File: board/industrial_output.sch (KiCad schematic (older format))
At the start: 3 parts, among them Q1501 NJT4031NT1G

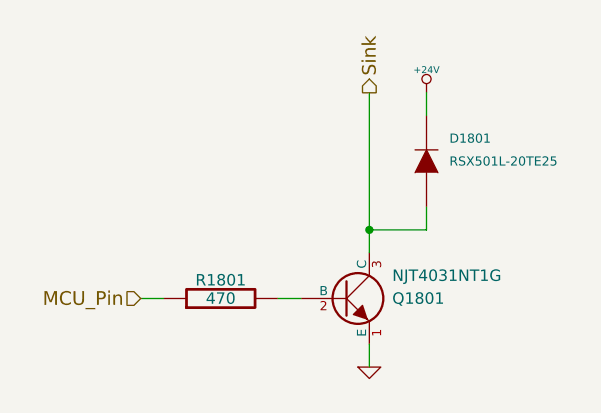
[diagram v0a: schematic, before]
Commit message: Selected Part Numbers for all Components
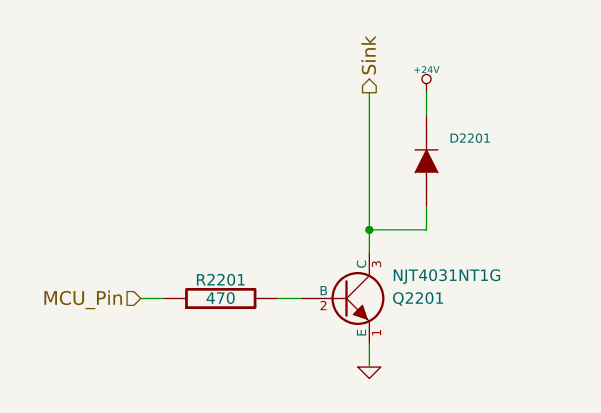
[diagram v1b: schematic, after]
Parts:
- D1501: Part Number (none) -> RSX501L-20TE25
- Q1501: Part Number (none) -> NJT4031NT1G
- R1501: Part Number (none) -> RC1608J471CS
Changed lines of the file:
@@
 $Descr A 11000 8500
 encoding utf-8
-Sheet 18 26
+Sheet 15 26
 Title "Industrial Digital Output"
 Date ""
@@
 AR Path="/52FAF275/52E6FDE0" Ref="Q2101"  Part="1"
 AR Path="/52FAF279/52E6FDE0" Ref="Q2201"  Part="1"
-F 0 "Q1801" H 5650 4500 50  0000 L CNN
+F 0 "Q2201" H 5650 4500 50  0000 L CNN
 F 1 "NJT4031NT1G" H 5650 4600 50  0000 L CNN
 F 2 "" H 5450 4500 60  0000 C CNN
 F 3 "" H 5450 4500 60  0000 C CNN
+F 4 "NJT4031NT1G" H 5450 4500 60  0001 C CNN "Part Number"
 	1    5450 4500
 	1    0    0    -1
@@
 AR Path="/52FAF275/52E6FDF4" Ref="R2101"  Part="1"
 AR Path="/52FAF279/52E6FDF4" Ref="R2201"  Part="1"
-F 0 "R1801" V 4980 4500 50  0000 C CNN
+F 0 "R2201" V 4980 4500 50  0000 C CNN
 F 1 "470" V 4900 4500 50  0000 C CNN
 F 2 "" H 4900 4500 60  0000 C CNN
 F 3 "" H 4900 4500 60  0000 C CNN
+F 4 "RC1608J471CS" V 4900 4500 60  0001 C CNN "Part Number"
 	1    4900 4500
 	0    -1   -1   0
@@
 	5150 4500 5250 4500
 $Comp
-L GND #PWR0160
+L GND #PWR0165
 U 1 1 52E6FE0A
 P 5550 4800
-AR Path="/52FAAFCB/52E6FE0A" Ref="#PWR0160"  Part="1"
-AR Path="/52FAC46B/52E6FE0A" Ref="#PWR0162"  Part="1"
-AR Path="/52FAD3BD/52E6FE0A" Ref="#PWR0164"  Part="1"
-AR Path="/52FAD3C1/52E6FE0A" Ref="#PWR0166"  Part="1"
-AR Path="/52FAF26D/52E6FE0A" Ref="#PWR0168"  Part="1"
-AR Path="/52FAF271/52E6FE0A" Ref="#PWR0170"  Part="1"
-AR Path="/52FAF275/52E6FE0A" Ref="#PWR0172"  Part="1"
-AR Path="/52FAF279/52E6FE0A" Ref="#PWR0174"  Part="1"
-F 0 "#PWR0166" H 5550 4800 30  0001 C CNN
+AR Path="/52FAAFCB/52E6FE0A" Ref="#PWR0165"  Part="1"
+AR Path="/52FAC46B/52E6FE0A" Ref="#PWR0167"  Part="1"
+AR Path="/52FAD3BD/52E6FE0A" Ref="#PWR0169"  Part="1"
+AR Path="/52FAD3C1/52E6FE0A" Ref="#PWR0171"  Part="1"
+AR Path="/52FAF26D/52E6FE0A" Ref="#PWR0173"  Part="1"
+AR Path="/52FAF271/52E6FE0A" Ref="#PWR0175"  Part="1"
+AR Path="/52FAF275/52E6FE0A" Ref="#PWR0177"  Part="1"
+AR Path="/52FAF279/52E6FE0A" Ref="#PWR0179"  Part="1"
+F 0 "#PWR0179" H 5550 4800 30  0001 C CNN
 F 1 "GND" H 5550 4730 30  0001 C CNN
 F 2 "" H 5550 4800 60  0000 C CNN
@@
 AR Path="/52FAF275/52E705F0" Ref="D2101"  Part="1"
 AR Path="/52FAF279/52E705F0" Ref="D2201"  Part="1"
-F 0 "D1801" V 5900 3800 40  0000 R CNN
-F 1 "RSX501L-20TE25" V 5800 3800 40  0000 R CNN
+F 0 "D2201" V 5900 3800 40  0000 R CNN
+F 1 "RSX501L-20TE25" V 5800 3800 40  0001 R CNN
 F 2 "" H 5800 3900 60  0000 C CNN
 F 3 "" H 5800 3900 60  0000 C CNN
+F 4 "RSX501L-20TE25" V 5800 3900 60  0001 C CNN "Part Number"
 	1    5800 3900
 	0    -1   -1   0
@@
 Connection ~ 5550 4200
 $Comp
-L +24V #PWR0161
+L +24V #PWR0166
 U 1 1 52E70673
 P 5800 3600
-AR Path="/52FAAFCB/52E70673" Ref="#PWR0161"  Part="1"
-AR Path="/52FAC46B/52E70673" Ref="#PWR0163"  Part="1"
-AR Path="/52FAD3BD/52E70673" Ref="#PWR0165"  Part="1"
-AR Path="/52FAD3C1/52E70673" Ref="#PWR0167"  Part="1"
-AR Path="/52FAF26D/52E70673" Ref="#PWR0169"  Part="1"
-AR Path="/52FAF271/52E70673" Ref="#PWR0171"  Part="1"
-AR Path="/52FAF275/52E70673" Ref="#PWR0173"  Part="1"
-AR Path="/52FAF279/52E70673" Ref="#PWR0175"  Part="1"
-F 0 "#PWR0167" H 5800 3550 20  0001 C CNN
+AR Path="/52FAAFCB/52E70673" Ref="#PWR0166"  Part="1"
+AR Path="/52FAC46B/52E70673" Ref="#PWR0168"  Part="1"
+AR Path="/52FAD3BD/52E70673" Ref="#PWR0170"  Part="1"
+AR Path="/52FAD3C1/52E70673" Ref="#PWR0172"  Part="1"
+AR Path="/52FAF26D/52E70673" Ref="#PWR0174"  Part="1"
+AR Path="/52FAF271/52E70673" Ref="#PWR0176"  Part="1"
+AR Path="/52FAF275/52E70673" Ref="#PWR0178"  Part="1"
+AR Path="/52FAF279/52E70673" Ref="#PWR0180"  Part="1"
+F 0 "#PWR0180" H 5800 3550 20  0001 C CNN
 F 1 "+24V" H 5800 3700 30  0000 C CNN
 F 2 "" H 5800 3600 60  0000 C CNN

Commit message: Industrial Output Ground, Associated Footprints
* Fixed an issue with the industrial output ground, it is now on the
  power ground rail.
* Associated most of the footprints, need to make a few.
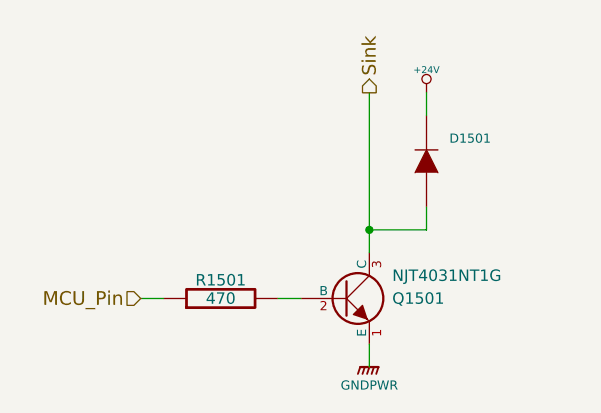
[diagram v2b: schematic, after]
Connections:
- net GND renamed GNDPWR
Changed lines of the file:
@@
 AR Path="/52FAF275/52E6FDE0" Ref="Q2101"  Part="1"
 AR Path="/52FAF279/52E6FDE0" Ref="Q2201"  Part="1"
-F 0 "Q2201" H 5650 4500 50  0000 L CNN
+F 0 "Q1501" H 5650 4500 50  0000 L CNN
 F 1 "NJT4031NT1G" H 5650 4600 50  0000 L CNN
 F 2 "" H 5450 4500 60  0000 C CNN
@@
 AR Path="/52FAF275/52E6FDF4" Ref="R2101"  Part="1"
 AR Path="/52FAF279/52E6FDF4" Ref="R2201"  Part="1"
-F 0 "R2201" V 4980 4500 50  0000 C CNN
+F 0 "R1501" V 4980 4500 50  0000 C CNN
 F 1 "470" V 4900 4500 50  0000 C CNN
 F 2 "" H 4900 4500 60  0000 C CNN
@@
 Wire Wire Line
 	5150 4500 5250 4500
-$Comp
-L GND #PWR0165
-U 1 1 52E6FE0A
-P 5550 4800
-AR Path="/52FAAFCB/52E6FE0A" Ref="#PWR0165"  Part="1"
-AR Path="/52FAC46B/52E6FE0A" Ref="#PWR0167"  Part="1"
-AR Path="/52FAD3BD/52E6FE0A" Ref="#PWR0169"  Part="1"
-AR Path="/52FAD3C1/52E6FE0A" Ref="#PWR0171"  Part="1"
-AR Path="/52FAF26D/52E6FE0A" Ref="#PWR0173"  Part="1"
-AR Path="/52FAF271/52E6FE0A" Ref="#PWR0175"  Part="1"
-AR Path="/52FAF275/52E6FE0A" Ref="#PWR0177"  Part="1"
-AR Path="/52FAF279/52E6FE0A" Ref="#PWR0179"  Part="1"
-F 0 "#PWR0179" H 5550 4800 30  0001 C CNN
-F 1 "GND" H 5550 4730 30  0001 C CNN
-F 2 "" H 5550 4800 60  0000 C CNN
-F 3 "" H 5550 4800 60  0000 C CNN
-	1    5550 4800
-	1    0    0    -1
-$EndComp
-Wire Wire Line
-	5550 4700 5550 4800
 Text HLabel 4550 4500 0    60   Input ~ 0
 MCU_Pin
@@
 AR Path="/52FAF275/52E705F0" Ref="D2101"  Part="1"
 AR Path="/52FAF279/52E705F0" Ref="D2201"  Part="1"
-F 0 "D2201" V 5900 3800 40  0000 R CNN
+F 0 "D1501" V 5900 3800 40  0000 R CNN
 F 1 "RSX501L-20TE25" V 5800 3800 40  0001 R CNN
 F 2 "" H 5800 3900 60  0000 C CNN
@@
 AR Path="/52FAF275/52E70673" Ref="#PWR0178"  Part="1"
 AR Path="/52FAF279/52E70673" Ref="#PWR0180"  Part="1"
-F 0 "#PWR0180" H 5800 3550 20  0001 C CNN
+F 0 "#PWR0166" H 5800 3550 20  0001 C CNN
 F 1 "+24V" H 5800 3700 30  0000 C CNN
 F 2 "" H 5800 3600 60  0000 C CNN
@@
 Wire Wire Line
 	5800 3600 5800 3700
+$Comp
+L GNDPWR #PWR?
+U 1 1 53019D4C
+P 5550 4800
+F 0 "#PWR?" H 5550 4850 40  0001 C CNN
+F 1 "GNDPWR" H 5550 4720 40  0000 C CNN
+F 2 "" H 5550 4800 60  0000 C CNN
+F 3 "" H 5550 4800 60  0000 C CNN
+	1    5550 4800
+	1    0    0    -1
+$EndComp
+Wire Wire Line
+	5550 4700 5550 4800
 $EndSCHEMATC

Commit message: Resolved issues while associating footprints.
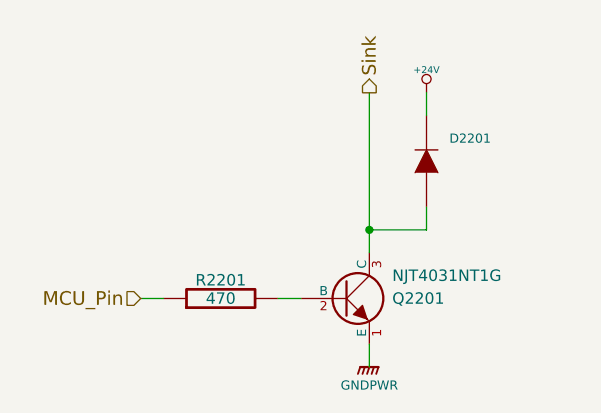
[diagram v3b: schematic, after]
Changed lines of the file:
@@
 AR Path="/52FAF275/52E6FDE0" Ref="Q2101"  Part="1"
 AR Path="/52FAF279/52E6FDE0" Ref="Q2201"  Part="1"
-F 0 "Q1501" H 5650 4500 50  0000 L CNN
+F 0 "Q2201" H 5650 4500 50  0000 L CNN
 F 1 "NJT4031NT1G" H 5650 4600 50  0000 L CNN
 F 2 "" H 5450 4500 60  0000 C CNN
@@
 AR Path="/52FAF275/52E6FDF4" Ref="R2101"  Part="1"
 AR Path="/52FAF279/52E6FDF4" Ref="R2201"  Part="1"
-F 0 "R1501" V 4980 4500 50  0000 C CNN
+F 0 "R2201" V 4980 4500 50  0000 C CNN
 F 1 "470" V 4900 4500 50  0000 C CNN
 F 2 "" H 4900 4500 60  0000 C CNN
@@
 AR Path="/52FAF275/52E705F0" Ref="D2101"  Part="1"
 AR Path="/52FAF279/52E705F0" Ref="D2201"  Part="1"
-F 0 "D1501" V 5900 3800 40  0000 R CNN
+F 0 "D2201" V 5900 3800 40  0000 R CNN
 F 1 "RSX501L-20TE25" V 5800 3800 40  0001 R CNN
 F 2 "" H 5800 3900 60  0000 C CNN
@@
 Connection ~ 5550 4200
 $Comp
-L +24V #PWR0166
+L +24V #PWR1501
 U 1 1 52E70673
 P 5800 3600
-AR Path="/52FAAFCB/52E70673" Ref="#PWR0166"  Part="1"
-AR Path="/52FAC46B/52E70673" Ref="#PWR0168"  Part="1"
-AR Path="/52FAD3BD/52E70673" Ref="#PWR0170"  Part="1"
-AR Path="/52FAD3C1/52E70673" Ref="#PWR0172"  Part="1"
-AR Path="/52FAF26D/52E70673" Ref="#PWR0174"  Part="1"
-AR Path="/52FAF271/52E70673" Ref="#PWR0176"  Part="1"
-AR Path="/52FAF275/52E70673" Ref="#PWR0178"  Part="1"
-AR Path="/52FAF279/52E70673" Ref="#PWR0180"  Part="1"
-F 0 "#PWR0166" H 5800 3550 20  0001 C CNN
+AR Path="/52FAAFCB/52E70673" Ref="#PWR1501"  Part="1"
+AR Path="/52FAC46B/52E70673" Ref="#PWR1601"  Part="1"
+AR Path="/52FAD3BD/52E70673" Ref="#PWR1701"  Part="1"
+AR Path="/52FAD3C1/52E70673" Ref="#PWR1801"  Part="1"
+AR Path="/52FAF26D/52E70673" Ref="#PWR1901"  Part="1"
+AR Path="/52FAF271/52E70673" Ref="#PWR2001"  Part="1"
+AR Path="/52FAF275/52E70673" Ref="#PWR2101"  Part="1"
+AR Path="/52FAF279/52E70673" Ref="#PWR2201"  Part="1"
+F 0 "#PWR2201" H 5800 3550 20  0001 C CNN
 F 1 "+24V" H 5800 3700 30  0000 C CNN
 F 2 "" H 5800 3600 60  0000 C CNN
@@
 	5800 3600 5800 3700
 $Comp
-L GNDPWR #PWR?
+L GNDPWR #PWR1502
 U 1 1 53019D4C
 P 5550 4800
-F 0 "#PWR?" H 5550 4850 40  0001 C CNN
+AR Path="/52FAAFCB/53019D4C" Ref="#PWR1502"  Part="1"
+AR Path="/52FAC46B/53019D4C" Ref="#PWR1602"  Part="1"
+AR Path="/52FAD3BD/53019D4C" Ref="#PWR1702"  Part="1"
+AR Path="/52FAD3C1/53019D4C" Ref="#PWR1802"  Part="1"
+AR Path="/52FAF26D/53019D4C" Ref="#PWR1902"  Part="1"
+AR Path="/52FAF271/53019D4C" Ref="#PWR2002"  Part="1"
+AR Path="/52FAF275/53019D4C" Ref="#PWR2102"  Part="1"
+AR Path="/52FAF279/53019D4C" Ref="#PWR2202"  Part="1"
+F 0 "#PWR2202" H 5550 4850 40  0001 C CNN
 F 1 "GNDPWR" H 5550 4720 40  0000 C CNN
 F 2 "" H 5550 4800 60  0000 C CNN

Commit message: Digikey Number + Link
Added a digikey part number and link to all components.
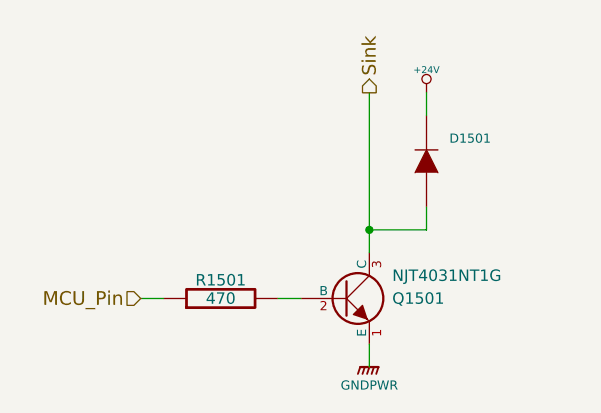
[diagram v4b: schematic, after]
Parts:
- D1501: Digikey Number (none) -> RSX501L-20TE25CT-ND; Part Number RSX501L-20TE25 -> (none)
- Q1501: Digikey Number (none) -> NJT4031NT1GOSCT-ND; Part Number NJT4031NT1G -> (none)
- R1501: Digikey Number (none) -> 1276-5054-1-ND; Part Number RC1608J471CS -> (none)
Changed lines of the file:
@@
 AR Path="/52FAF275/52E6FDE0" Ref="Q2101"  Part="1"
 AR Path="/52FAF279/52E6FDE0" Ref="Q2201"  Part="1"
-F 0 "Q2201" H 5650 4500 50  0000 L CNN
+AR Path="/52E6FDE0" Ref="Q2201"  Part="1"
+F 0 "Q1501" H 5650 4500 50  0000 L CNN
 F 1 "NJT4031NT1G" H 5650 4600 50  0000 L CNN
 F 2 "" H 5450 4500 60  0000 C CNN
-F 3 "" H 5450 4500 60  0000 C CNN
-F 4 "NJT4031NT1G" H 5450 4500 60  0001 C CNN "Part Number"
+F 3 "http://www.digikey.ca/product-detail/en/NJT4031NT1G/NJT4031NT1GOSCT-ND/1693205" H 5450 4500 60  0001 C CNN
+F 4 "NJT4031NT1GOSCT-ND" H 6900 4550 60  0001 C CNN "Digikey Number"
 	1    5450 4500
 	1    0    0    -1
@@
 AR Path="/52FAF275/52E6FDF4" Ref="R2101"  Part="1"
 AR Path="/52FAF279/52E6FDF4" Ref="R2201"  Part="1"
-F 0 "R2201" V 4980 4500 50  0000 C CNN
+F 0 "R1501" V 4980 4500 50  0000 C CNN
 F 1 "470" V 4900 4500 50  0000 C CNN
 F 2 "" H 4900 4500 60  0000 C CNN
-F 3 "" H 4900 4500 60  0000 C CNN
-F 4 "RC1608J471CS" V 4900 4500 60  0001 C CNN "Part Number"
+F 3 "http://www.digikey.ca/product-detail/en/RC1608J471CS/1276-5054-1-ND/3968026" H 4900 4500 60  0001 C CNN
+F 4 "1276-5054-1-ND" H 6900 4550 60  0001 C CNN "Digikey Number"
 	1    4900 4500
 	0    -1   -1   0
@@
 AR Path="/52FAF275/52E705F0" Ref="D2101"  Part="1"
 AR Path="/52FAF279/52E705F0" Ref="D2201"  Part="1"
-F 0 "D2201" V 5900 3800 40  0000 R CNN
+AR Path="/52E705F0" Ref="D2201"  Part="1"
+F 0 "D1501" V 5900 3800 40  0000 R CNN
 F 1 "RSX501L-20TE25" V 5800 3800 40  0001 R CNN
 F 2 "" H 5800 3900 60  0000 C CNN
-F 3 "" H 5800 3900 60  0000 C CNN
-F 4 "RSX501L-20TE25" V 5800 3900 60  0001 C CNN "Part Number"
+F 3 "http://www.digikey.ca/product-detail/en/RSX501L-20TE25/RSX501L-20TE25CT-ND/2095553" H 5800 3900 60  0001 C CNN
+F 4 "RSX501L-20TE25CT-ND" H 6900 4550 60  0001 C CNN "Digikey Number"
 	1    5800 3900
 	0    -1   -1   0
@@
 AR Path="/52FAF275/52E70673" Ref="#PWR2101"  Part="1"
 AR Path="/52FAF279/52E70673" Ref="#PWR2201"  Part="1"
-F 0 "#PWR2201" H 5800 3550 20  0001 C CNN
+F 0 "#PWR1501" H 5800 3550 20  0001 C CNN
 F 1 "+24V" H 5800 3700 30  0000 C CNN
 F 2 "" H 5800 3600 60  0000 C CNN
@@
 AR Path="/52FAF275/53019D4C" Ref="#PWR2102"  Part="1"
 AR Path="/52FAF279/53019D4C" Ref="#PWR2202"  Part="1"
-F 0 "#PWR2202" H 5550 4850 40  0001 C CNN
+F 0 "#PWR1502" H 5550 4850 40  0001 C CNN
 F 1 "GNDPWR" H 5550 4720 40  0000 C CNN
 F 2 "" H 5550 4800 60  0000 C CNN

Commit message: Prepared components/footprints for PCB Layout.
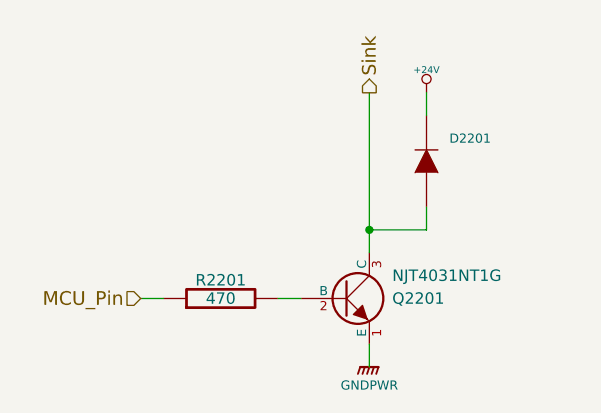
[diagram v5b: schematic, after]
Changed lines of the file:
@@
 AR Path="/52FAF275/52E6FDE0" Ref="Q2101"  Part="1"
 AR Path="/52FAF279/52E6FDE0" Ref="Q2201"  Part="1"
-AR Path="/52E6FDE0" Ref="Q2201"  Part="1"
-F 0 "Q1501" H 5650 4500 50  0000 L CNN
+F 0 "Q2201" H 5650 4500 50  0000 L CNN
 F 1 "NJT4031NT1G" H 5650 4600 50  0000 L CNN
 F 2 "" H 5450 4500 60  0000 C CNN
@@
 AR Path="/52FAF275/52E6FDF4" Ref="R2101"  Part="1"
 AR Path="/52FAF279/52E6FDF4" Ref="R2201"  Part="1"
-F 0 "R1501" V 4980 4500 50  0000 C CNN
+F 0 "R2201" V 4980 4500 50  0000 C CNN
 F 1 "470" V 4900 4500 50  0000 C CNN
 F 2 "" H 4900 4500 60  0000 C CNN
@@
 AR Path="/52FAF275/52E705F0" Ref="D2101"  Part="1"
 AR Path="/52FAF279/52E705F0" Ref="D2201"  Part="1"
-AR Path="/52E705F0" Ref="D2201"  Part="1"
-F 0 "D1501" V 5900 3800 40  0000 R CNN
+F 0 "D2201" V 5900 3800 40  0000 R CNN
 F 1 "RSX501L-20TE25" V 5800 3800 40  0001 R CNN
 F 2 "" H 5800 3900 60  0000 C CNN
@@
 Connection ~ 5550 4200
 $Comp
-L +24V #PWR1501
+L +24V #PWR0165
 U 1 1 52E70673
 P 5800 3600
-AR Path="/52FAAFCB/52E70673" Ref="#PWR1501"  Part="1"
-AR Path="/52FAC46B/52E70673" Ref="#PWR1601"  Part="1"
-AR Path="/52FAD3BD/52E70673" Ref="#PWR1701"  Part="1"
-AR Path="/52FAD3C1/52E70673" Ref="#PWR1801"  Part="1"
-AR Path="/52FAF26D/52E70673" Ref="#PWR1901"  Part="1"
-AR Path="/52FAF271/52E70673" Ref="#PWR2001"  Part="1"
-AR Path="/52FAF275/52E70673" Ref="#PWR2101"  Part="1"
-AR Path="/52FAF279/52E70673" Ref="#PWR2201"  Part="1"
-F 0 "#PWR1501" H 5800 3550 20  0001 C CNN
+AR Path="/52FAAFCB/52E70673" Ref="#PWR0165"  Part="1"
+AR Path="/52FAC46B/52E70673" Ref="#PWR0167"  Part="1"
+AR Path="/52FAD3BD/52E70673" Ref="#PWR0169"  Part="1"
+AR Path="/52FAD3C1/52E70673" Ref="#PWR0171"  Part="1"
+AR Path="/52FAF26D/52E70673" Ref="#PWR0173"  Part="1"
+AR Path="/52FAF271/52E70673" Ref="#PWR0175"  Part="1"
+AR Path="/52FAF275/52E70673" Ref="#PWR0177"  Part="1"
+AR Path="/52FAF279/52E70673" Ref="#PWR0179"  Part="1"
+F 0 "#PWR0179" H 5800 3550 20  0001 C CNN
 F 1 "+24V" H 5800 3700 30  0000 C CNN
 F 2 "" H 5800 3600 60  0000 C CNN
@@
 	5800 3600 5800 3700
 $Comp
-L GNDPWR #PWR1502
+L GNDPWR #PWR0166
 U 1 1 53019D4C
 P 5550 4800
-AR Path="/52FAAFCB/53019D4C" Ref="#PWR1502"  Part="1"
-AR Path="/52FAC46B/53019D4C" Ref="#PWR1602"  Part="1"
-AR Path="/52FAD3BD/53019D4C" Ref="#PWR1702"  Part="1"
-AR Path="/52FAD3C1/53019D4C" Ref="#PWR1802"  Part="1"
-AR Path="/52FAF26D/53019D4C" Ref="#PWR1902"  Part="1"
-AR Path="/52FAF271/53019D4C" Ref="#PWR2002"  Part="1"
-AR Path="/52FAF275/53019D4C" Ref="#PWR2102"  Part="1"
-AR Path="/52FAF279/53019D4C" Ref="#PWR2202"  Part="1"
-F 0 "#PWR1502" H 5550 4850 40  0001 C CNN
+AR Path="/52FAAFCB/53019D4C" Ref="#PWR0166"  Part="1"
+AR Path="/52FAC46B/53019D4C" Ref="#PWR0168"  Part="1"
+AR Path="/52FAD3BD/53019D4C" Ref="#PWR0170"  Part="1"
+AR Path="/52FAD3C1/53019D4C" Ref="#PWR0172"  Part="1"
+AR Path="/52FAF26D/53019D4C" Ref="#PWR0174"  Part="1"
+AR Path="/52FAF271/53019D4C" Ref="#PWR0176"  Part="1"
+AR Path="/52FAF275/53019D4C" Ref="#PWR0178"  Part="1"
+AR Path="/52FAF279/53019D4C" Ref="#PWR0180"  Part="1"
+F 0 "#PWR0180" H 5550 4850 40  0001 C CNN
 F 1 "GNDPWR" H 5550 4720 40  0000 C CNN
 F 2 "" H 5550 4800 60  0000 C CNN

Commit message: Removed PWR-GND, change footprint for a bunch of capacitors
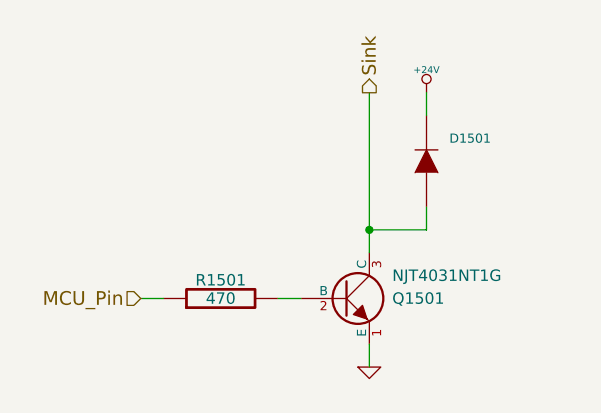
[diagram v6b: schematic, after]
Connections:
- net GNDPWR renamed GND
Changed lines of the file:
@@
 AR Path="/52FAF275/52E6FDE0" Ref="Q2101"  Part="1"
 AR Path="/52FAF279/52E6FDE0" Ref="Q2201"  Part="1"
-F 0 "Q2201" H 5650 4500 50  0000 L CNN
+F 0 "Q1501" H 5650 4500 50  0000 L CNN
 F 1 "NJT4031NT1G" H 5650 4600 50  0000 L CNN
 F 2 "" H 5450 4500 60  0000 C CNN
@@
 AR Path="/52FAF275/52E6FDF4" Ref="R2101"  Part="1"
 AR Path="/52FAF279/52E6FDF4" Ref="R2201"  Part="1"
-F 0 "R2201" V 4980 4500 50  0000 C CNN
+F 0 "R1501" V 4980 4500 50  0000 C CNN
 F 1 "470" V 4900 4500 50  0000 C CNN
 F 2 "" H 4900 4500 60  0000 C CNN
@@
 AR Path="/52FAF275/52E705F0" Ref="D2101"  Part="1"
 AR Path="/52FAF279/52E705F0" Ref="D2201"  Part="1"
-F 0 "D2201" V 5900 3800 40  0000 R CNN
+F 0 "D1501" V 5900 3800 40  0000 R CNN
 F 1 "RSX501L-20TE25" V 5800 3800 40  0001 R CNN
 F 2 "" H 5800 3900 60  0000 C CNN
@@
 Connection ~ 5550 4200
 $Comp
-L +24V #PWR0165
+L +24V #PWR0164
 U 1 1 52E70673
 P 5800 3600
-AR Path="/52FAAFCB/52E70673" Ref="#PWR0165"  Part="1"
-AR Path="/52FAC46B/52E70673" Ref="#PWR0167"  Part="1"
-AR Path="/52FAD3BD/52E70673" Ref="#PWR0169"  Part="1"
-AR Path="/52FAD3C1/52E70673" Ref="#PWR0171"  Part="1"
-AR Path="/52FAF26D/52E70673" Ref="#PWR0173"  Part="1"
-AR Path="/52FAF271/52E70673" Ref="#PWR0175"  Part="1"
-AR Path="/52FAF275/52E70673" Ref="#PWR0177"  Part="1"
-AR Path="/52FAF279/52E70673" Ref="#PWR0179"  Part="1"
-F 0 "#PWR0179" H 5800 3550 20  0001 C CNN
+AR Path="/52FAAFCB/52E70673" Ref="#PWR0164"  Part="1"
+AR Path="/52FAC46B/52E70673" Ref="#PWR0166"  Part="1"
+AR Path="/52FAD3BD/52E70673" Ref="#PWR0168"  Part="1"
+AR Path="/52FAD3C1/52E70673" Ref="#PWR0170"  Part="1"
+AR Path="/52FAF26D/52E70673" Ref="#PWR0172"  Part="1"
+AR Path="/52FAF271/52E70673" Ref="#PWR0174"  Part="1"
+AR Path="/52FAF275/52E70673" Ref="#PWR0176"  Part="1"
+AR Path="/52FAF279/52E70673" Ref="#PWR0178"  Part="1"
+F 0 "#PWR0178" H 5800 3550 20  0001 C CNN
 F 1 "+24V" H 5800 3700 30  0000 C CNN
 F 2 "" H 5800 3600 60  0000 C CNN
@@
 Wire Wire Line
 	5800 3600 5800 3700
+Wire Wire Line
+	5550 4700 5550 4800
 $Comp
-L GNDPWR #PWR0166
-U 1 1 53019D4C
+L GND #PWR0165
+U 1 1 5311E771
 P 5550 4800
-AR Path="/52FAAFCB/53019D4C" Ref="#PWR0166"  Part="1"
-AR Path="/52FAC46B/53019D4C" Ref="#PWR0168"  Part="1"
-AR Path="/52FAD3BD/53019D4C" Ref="#PWR0170"  Part="1"
-AR Path="/52FAD3C1/53019D4C" Ref="#PWR0172"  Part="1"
-AR Path="/52FAF26D/53019D4C" Ref="#PWR0174"  Part="1"
-AR Path="/52FAF271/53019D4C" Ref="#PWR0176"  Part="1"
-AR Path="/52FAF275/53019D4C" Ref="#PWR0178"  Part="1"
-AR Path="/52FAF279/53019D4C" Ref="#PWR0180"  Part="1"
-F 0 "#PWR0180" H 5550 4850 40  0001 C CNN
-F 1 "GNDPWR" H 5550 4720 40  0000 C CNN
+AR Path="/52FAAFCB/5311E771" Ref="#PWR0165"  Part="1"
+AR Path="/52FAC46B/5311E771" Ref="#PWR0167"  Part="1"
+AR Path="/52FAD3BD/5311E771" Ref="#PWR0169"  Part="1"
+AR Path="/52FAD3C1/5311E771" Ref="#PWR0171"  Part="1"
+AR Path="/52FAF26D/5311E771" Ref="#PWR0173"  Part="1"
+AR Path="/52FAF271/5311E771" Ref="#PWR0175"  Part="1"
+AR Path="/52FAF275/5311E771" Ref="#PWR0177"  Part="1"
+AR Path="/52FAF279/5311E771" Ref="#PWR0179"  Part="1"
+F 0 "#PWR0179" H 5550 4800 30  0001 C CNN
+F 1 "GND" H 5550 4730 30  0001 C CNN
 F 2 "" H 5550 4800 60  0000 C CNN
 F 3 "" H 5550 4800 60  0000 C CNN
@@
 	1    0    0    -1
 $EndComp
-Wire Wire Line
-	5550 4700 5550 4800
 $EndSCHEMATC
